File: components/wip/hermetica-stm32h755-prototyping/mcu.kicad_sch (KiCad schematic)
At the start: 165 parts, among them J1 CONNECTOR-DEBUG-SPECIFIC-ARM, J10 Conn_01x01, J100 Conn_01x01, J101 Conn_01x01, J102 Conn_01x01, J103 Conn_01x01, J104 Conn_01x01, J105 Conn_01x01, J106 Conn_01x01, J107 Conn_01x01, J108 Conn_01x01, J109 Conn_01x01, J11 Conn_01x01, J111 Conn_01x01, J112 Conn_01x01, J113 Conn_01x01, J114 Conn_01x01, J115 Conn_01x01, J116 Conn_01x01, J117 Conn_01x01, J118 Conn_01x01, J119 Conn_01x01, J12 Conn_01x01, J120 Conn_01x01, J121 Conn_01x01, J122 Conn_01x01, J123 Conn_01x01, J124 Conn_01x01, J125 Conn_01x01, J126 Conn_01x01, J127 Conn_01x01, J13 Conn_01x01, J130 Conn_01x01, J131 Conn_01x01, J132 Conn_01x01, J133 Conn_01x01, J134 Conn_01x01, J135 Conn_01x01, J14 Conn_01x01, J15 Conn_01x01, J16 Conn_01x01, J17 Conn_01x01, J18 Conn_01x01, J19 Conn_01x01, J2 Conn_01x01, J20 Conn_01x01, J21 Conn_01x01, J22 Conn_01x01, J23 Conn_01x01, J24 Conn_01x01, J25 Conn_01x01, J26 Conn_01x01, J27 Conn_01x01, J30 Conn_01x01, J31 Conn_01x01, J32 Conn_01x01, J33 Conn_01x01, J34 Conn_01x01, J35 Conn_01x01, J36 Conn_01x01, J37 Conn_01x01, J38 Conn_01x01, J39 Conn_01x01, J4 Conn_01x01, J40 Conn_01x01, J41 Conn_01x01, J42 Conn_01x01, J43 Conn_01x01, J44 Conn_01x01, J45 Conn_01x01, J47 Conn_01x01, J48 Conn_01x01, J49 Conn_01x01, J5 Conn_01x01, J50 Conn_01x01, J53 Conn_01x01, J54 Conn_01x01, J55 Conn_01x01, J56 Conn_01x01, J57 Conn_01x01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

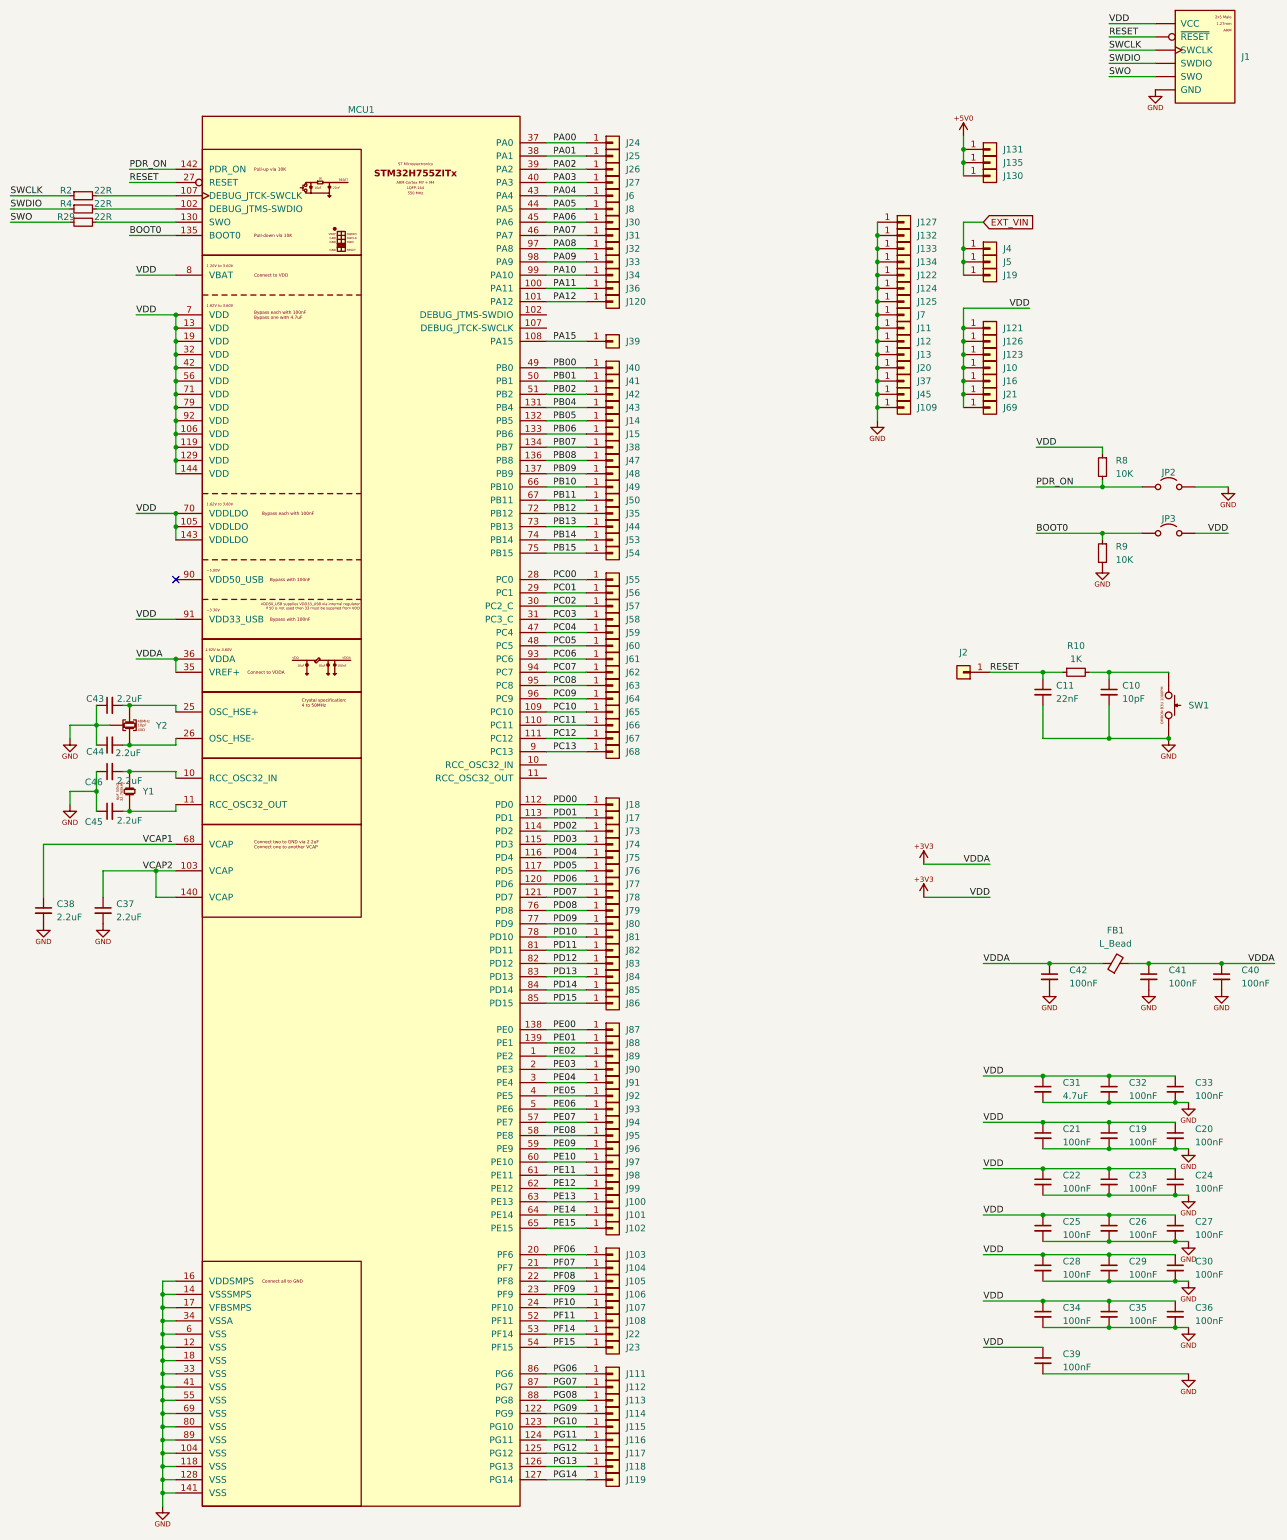
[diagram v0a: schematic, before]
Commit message: STM32H755ZIT6 dev board
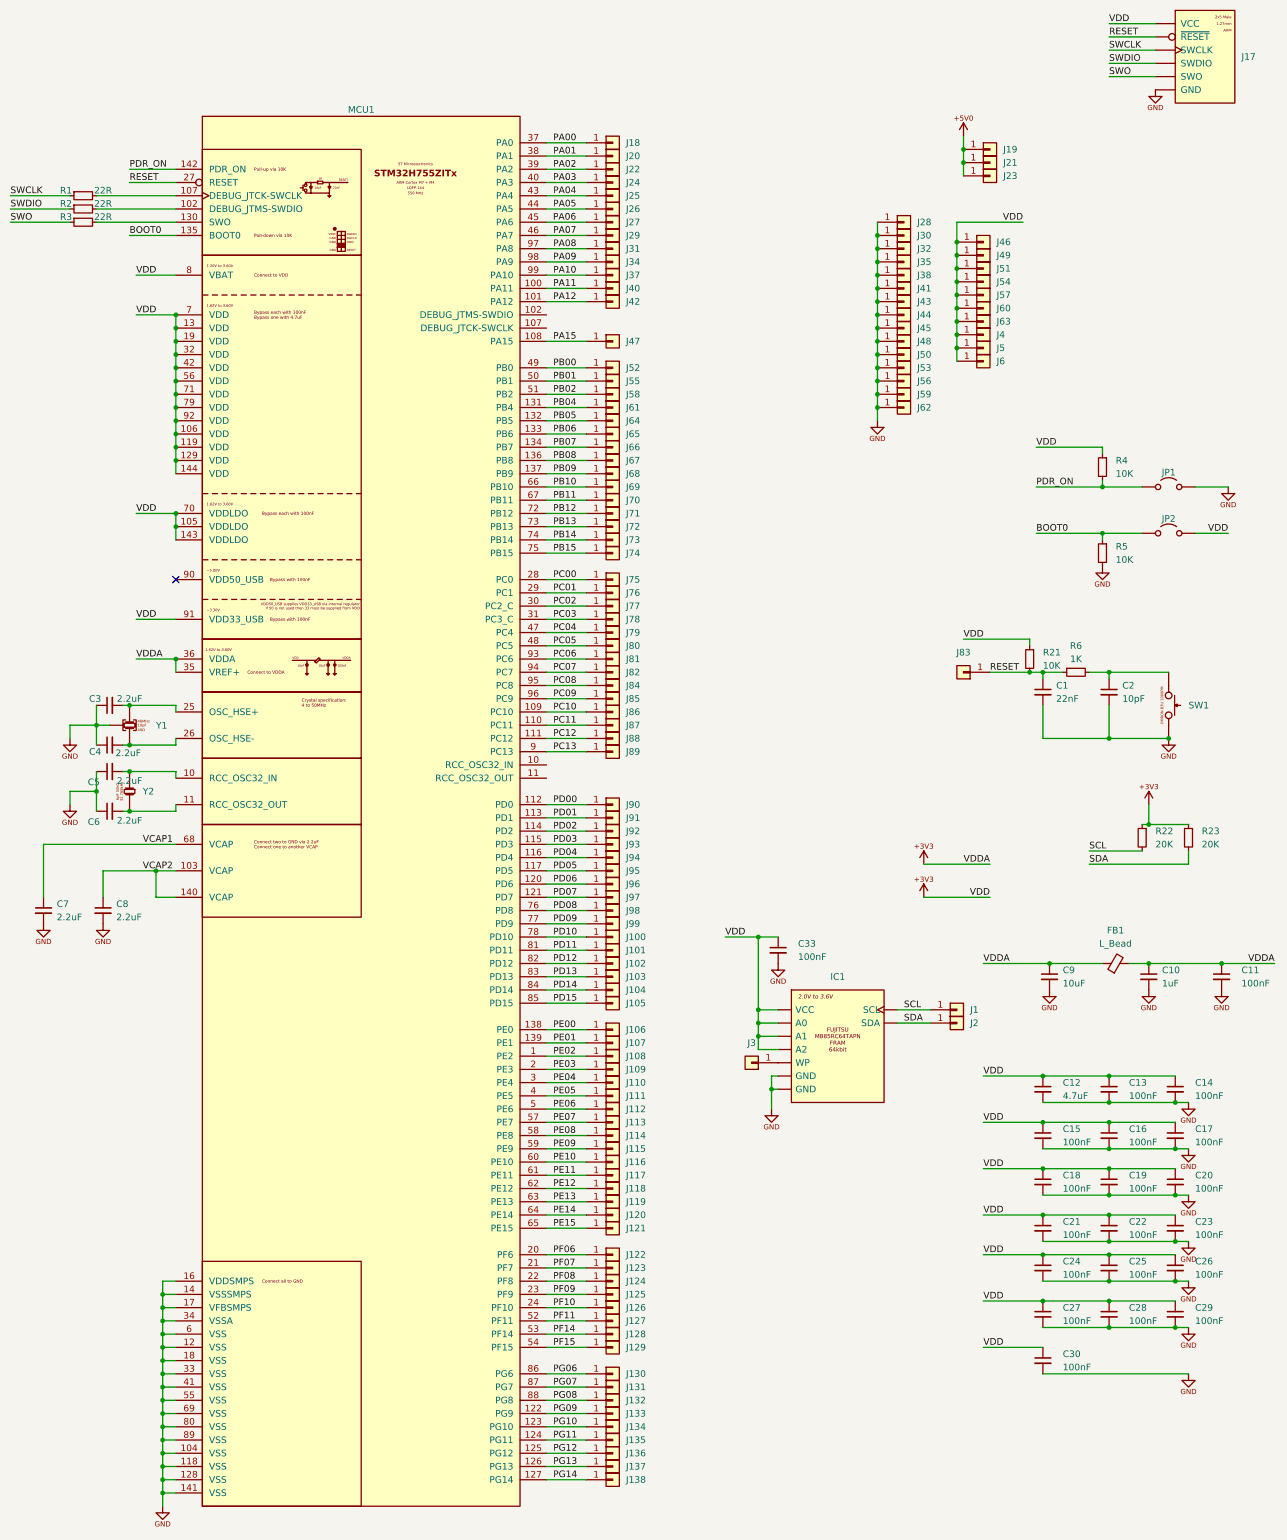
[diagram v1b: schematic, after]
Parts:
- removed J19: Conn_01x01, djStandard:CONNECTOR-PCB-HANDSOLDER-01X01-FEMALE, symbol Connector_Generic:Conn_01x01
- added C33: 100nF, djStandard:C_0402_1005Metric, symbol DJ:C
- added IC1: FUJITSU-MB85RC64TAPN, djStandard:FUJITSU-MB85RC64TAPN-SON8, symbol DJ:FUJITSU-MB85RC64TAPN-SON8
- added J1, J2, J3, J6: Conn_01x01, djStandard:CONNECTOR-PCB-HANDSOLDER-01X01-FEMALE, symbol Connector_Generic:Conn_01x01
- added R21: 10K, djStandard:R_0402_1005Metric, symbol DJ:R
- added R22, R23: 20K, djStandard:R_0402_1005Metric, symbol DJ:R
- C10: renamed from C41; value 100nF -> 1uF
- C9: renamed from C42; value 100nF -> 10uF
- renumbered C11 to C1, C40 to C11, C31 to C12, C32 to C13, C33 to C14, C21 to C15, C19 to C16, C20 to C17, C22 to C18, C23 to C19, C10 to C2, C24 to C20, C25 to C21, C26 to C22, C27 to C23, C28 to C24, C29 to C25, C30 to C26, C34 to C27, C35 to C28, C36 to C29, C43 to C3, C39 to C30, C44 to C4, C46 to C5, C45 to C6, C38 to C7, C37 to C8, J81 to J100, J82 to J101, J83 to J102, J84 to J103, J85 to J104, J86 to J105, J87 to J106, J88 to J107, J89 to J108, J90 to J109, J91 to J110, J92 to J111, J93 to J112, J94 to J113, J95 to J114, J96 to J115, J97 to J116, J98 to J117, J99 to J118, J100 to J119, J101 to J120, J102 to J121, J103 to J122, J104 to J123, J105 to J124, J106 to J125, J107 to J126, J108 to J127, J22 to J128, J23 to J129, J111 to J130, J112 to J131, J113 to J132, J114 to J133, J115 to J134, J116 to J135, J117 to J136, J118 to J137, J119 to J138, J1 to J17, J24 to J18, J131 to J19, J25 to J20, J135 to J21, J26 to J22, J130 to J23, J27 to J24, J6 to J25, J8 to J26, J30 to J27, J127 to J28, J31 to J29, J132 to J30, J32 to J31, J133 to J32, J33 to J34, J134 to J35, J34 to J37, J122 to J38, J36 to J40, J124 to J41, J120 to J42, J125 to J43, J7 to J44, J11 to J45, J121 to J46, J39 to J47, J12 to J48, J126 to J49, J13 to J50, J123 to J51, J40 to J52, J20 to J53, J10 to J54, J41 to J55, J37 to J56, J16 to J57, J42 to J58, J45 to J59, J21 to J60, J43 to J61, J109 to J62, J69 to J63, J14 to J64, J15 to J65, J38 to J66, J47 to J67, J48 to J68, J49 to J69, J50 to J70, J35 to J71, J44 to J72, J53 to J73, J54 to J74, J55 to J75, J56 to J76, J57 to J77, J58 to J78, J59 to J79, J60 to J80, J61 to J81, J62 to J82, J2 to J83, J63 to J84, J64 to J85, J65 to J86, J66 to J87, J67 to J88, J68 to J89, J18 to J90, J17 to J91, J73 to J92, J74 to J93, J75 to J94, J76 to J95, J77 to J96, J78 to J97, J79 to J98, J80 to J99, JP2 to JP1, JP3 to JP2, R2 to R1, R4 to R2, R29 to R3, R8 to R4, R9 to R5, R10 to R6, Y2 to Y1, Y1 to Y2
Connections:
- net EXT_VIN is gone; now on net +3V3: J4.1 (Pin_1), J5.1 (Pin_1)
- net +3V3: now also C33.1, IC1.1 (A0), IC1.2 (A1), IC1.3 (A2), IC1.8 (VCC), J6.1 (Pin_1), R21.1, R22.1, R23.1
- net GND: now also C33.2, IC1.4 (GND), IC1.9 (GND)
- net RESET: now also R21.2
- new net: IC1.7 (WP), J3.1 (Pin_1)
- new net SCL: IC1.6 (SCL), J1.1 (Pin_1), R22.2
- new net SDA: IC1.5 (SDA), J2.1 (Pin_1), R23.2
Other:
- moved on the sheet: J46, J49, J51, J54, J57, J60, J63
